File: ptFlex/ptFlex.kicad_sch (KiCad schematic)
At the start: 75 parts, among them J1 6 Pin Male Header, J2 8 Pin Male Header, J4 Qwiic, J5 3 Pin Male Header, J6 Barrel_Jack_Switch, Q1 BSS138, Q2 BSS138, Q3 MMBT3904, Q4 MMBT3904, Q5 DMP2004K-7, SW1 Reset Switch, U1 LP3985IM5-3.3/NOPB, U2 ATMega 328p-AU, U3 SA818S-V, U4 ATGM336H-5N31, U5 LM1086-5.0, U6 BME280, Y1 8MHz

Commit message: Schematic mostly revised for v2.0
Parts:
- removed ANT2a1, ANT2b1: VHF Test Point, Custom DS:Small Test Point Pin, symbol Connector_Generic:Conn_01x01
- removed J2: 8 Pin Male Header, Connector_PinHeader_2.54mm:PinHeader_2x04_P2.54mm_Vertical, symbol Connector_Generic:Conn_02x04_Odd_Even
- Y1: value 8MHz -> 16MHz
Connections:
- net +3.3V: no longer C12.1, R7.1, U2.18 (AVCC), U2.4 (VCC), U2.6 (VCC)
- net BATT-SENSE: no longer C2.1, R2.1, R3.2
- net GND: now also SW1.1 (A); no longer SW1.2 (B)
- net GPS-RX: no longer U4.2 (TXD)
- net GPS-TX: no longer U4.3 (RXD)
- net RESET: now also SW1.2 (B)
- net SCL: no longer R8.2
- net SDA: no longer R9.2
- net at C1.1, U5.3 (VI): now also D4.1 (K), R2.2; no longer J6.1
- net at Q2.2 (S), R12.1: now also U4.2 (TXD)
- net at C20.1, Q5.3 (D), U4.8 (VCC): now also C12.1
- net at Q1.2 (S), R10.1: now also U4.3 (RXD)
- net at J5.1 (Pin_1): now also U2.31 (PD1)
- net at J5.2 (Pin_2): now also U2.30 (PD0)
- net at J4.3 (Pin_3), U6.3 (SDI): now also R9.2
- net at J4.4 (Pin_4), U6.4 (SCK): now also R8.2
- net at D4.2 (A): now also J6.1
- net PIEZO: now reaches R1.2
- net +BATT renamed +5V
- net +5V: now also R7.1, U2.18 (AVCC), U2.4 (VCC), U2.6 (VCC); no longer D4.1 (K), R2.2
- new net: C2.1, R2.1, R3.2
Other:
- moved on the sheet: ANT1, ANT2, C1, C10, C11, C12, C13, C14, C15, C16, C17, C18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

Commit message: PCB nearing final
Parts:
- removed SW1: Reset Switch, Button_Switch_SMD:SW_SPST_PTS647_Sx38, symbol Switch:SW_SPST
- ANT2: value SMA Edge Mount (Optional) -> SMA Connector; footprint Connector_Coaxial:SMA_Samtec_SMA-J-P-H-ST-EM1_EdgeMount -> Connector_Coaxial:SMB_Jack_Vertical; Digikey CON-SMA-EDGE-S-ND -> (none)
- C21: value 2.2uF -> 47uF; Digikey 445-1420-1-ND -> (none); LCSC C107128 -> (none)
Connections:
- net BATT-SENSE: now also C2.1, R2.1, R3.2
- net DIG-PTT: no longer R20.2, R4.1, U2.32 (PD2)
- net GPS-RX: now also Q2.3 (D), R13.1
- net GPS-TX: now also Q1.3 (D), R11.1
- net PIEZO: now also U2.9 (PD5)
- net XMIT-POWERSAVE: now reaches R22.2, U2.2 (PD4), U3.6 (POWER_SAVE)
- net XMIT-TX-AUDIO: now reaches R16.1, U2.1 (PD3)
- net XMIT-TX: now reaches U2.13 (PB1), U3.16 (RX_DATA)
- net XMIT-RX: now reaches U2.14 (PB2), U3.17 (TX_DATA)
- new net XMIT-PTT: R20.2, R4.1, U2.32 (PD2)
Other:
- moved on the sheet: C2, C20, D4, J6, Q2, R12, R13, R2, R22, R3

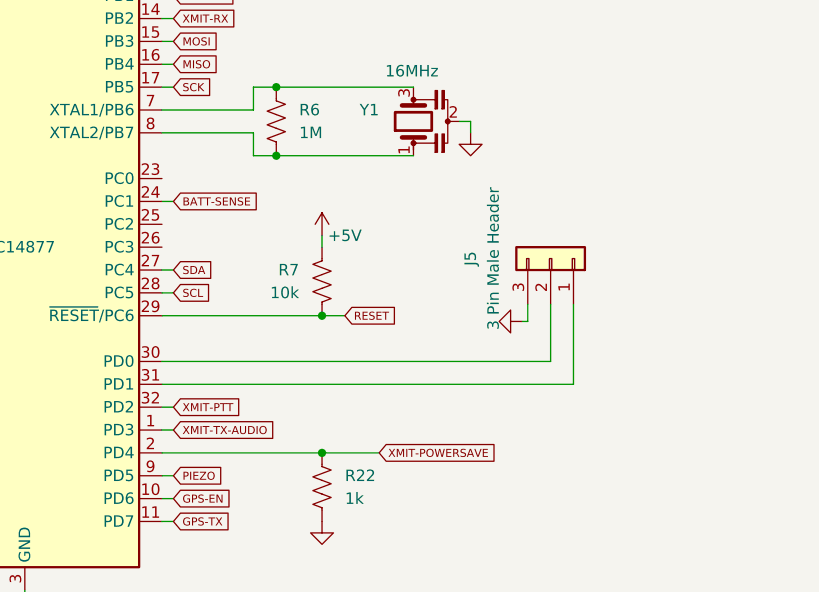
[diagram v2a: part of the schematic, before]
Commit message: Back filed old versions of PCB from the ptFlex-hardware project into this repo. Shrunk the PCB down by 5mm.
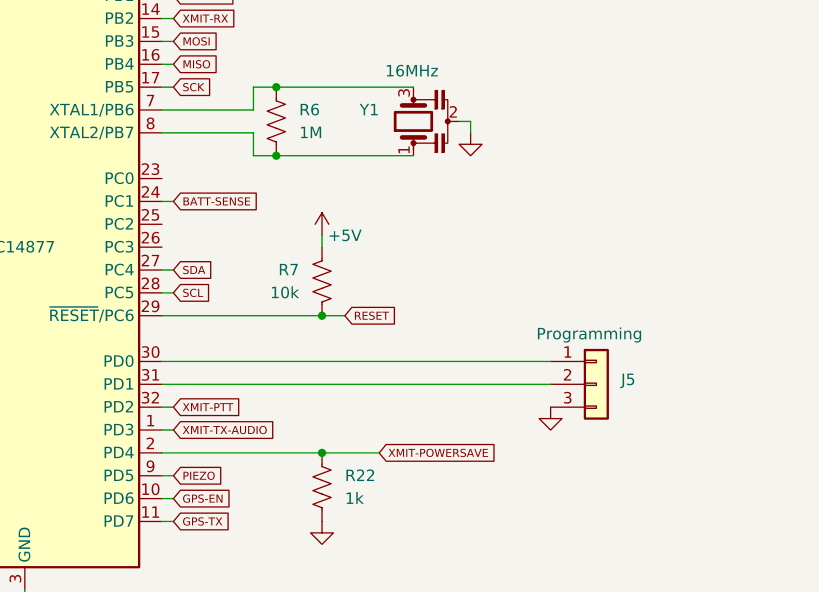
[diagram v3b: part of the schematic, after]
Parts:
- J5: value 3 Pin Male Header -> Programming
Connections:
- net at J5.1 (Pin_1): now also U2.30 (PD0); no longer U2.31 (PD1)
- net at J5.2 (Pin_2): now also U2.31 (PD1); no longer U2.30 (PD0)
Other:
- moved on the sheet: J5
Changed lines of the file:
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@@
 	(wire
 		(pts
-			(xy 163.83 67.31) (xy 163.83 69.215)
-		)
-		(stroke
-			(width 0)
-			(type default)
-		)
-	)
-	(wire
-		(pts
 			(xy 269.24 73.66) (xy 274.32 73.66)
 		)
@@
 	(wire
 		(pts
-			(xy 163.83 69.215) (xy 163.195 69.215)
-		)
-		(stroke
-			(width 0)
-			(type default)
-		)
-	)
-	(wire
-		(pts
 			(xy 36.83 48.26) (xy 36.83 52.07)
 		)
@@
 	(wire
 		(pts
-			(xy 166.37 67.31) (xy 166.37 73.66)
-		)
-		(stroke
-			(width 0)
-			(type default)
-		)
-	)
-	(wire
-		(pts
 			(xy 351.79 133.35) (xy 351.79 135.89)
 		)
@@
 	(wire
 		(pts
-			(xy 168.91 67.31) (xy 168.91 76.2)
-		)
-		(stroke
-			(width 0)
-			(type default)
-		)
-	)
-	(wire
-		(pts
-			(xy 123.19 76.2) (xy 168.91 76.2)
+			(xy 123.19 76.2) (xy 166.37 76.2)
 		)
 		(stroke
@@
 	(symbol
 		(lib_id "Connector_Generic:Conn_01x03")
-		(at 166.37 62.23 270)
-		(mirror x)
+		(at 171.45 76.2 0)
 		(unit 1)
 		(exclude_from_sim no)
@@
 		(dnp no)
 		(property "Reference" "J5"
-			(at 157.48 62.23 0)
+			(at 175.006 75.692 0)
 			(effects
 				(font
@@
 			)
 		)
-		(property "Value" "3 Pin Male Header"
-			(at 160.02 62.23 0)
+		(property "Value" "Programming"
+			(at 170.688 70.612 0)
 			(effects
 				(font
@@
 		)
 		(property "Footprint" "Connector_PinHeader_2.54mm:PinHeader_1x03_P2.54mm_Vertical"
-			(at 166.37 62.23 0)
+			(at 171.45 76.2 0)
 			(effects
 				(font
@@
 		)
 		(property "Datasheet" "~"
-			(at 166.37 62.23 0)
+			(at 171.45 76.2 0)
 			(effects
 				(font
@@
 		)
 		(property "Description" "Generic connector, single row, 01x03, script generated (kicad-library-utils/schlib/autogen/connector/)"
-			(at 166.37 62.23 0)
+			(at 171.45 76.2 0)
 			(effects
 				(font
@@
 		)
 		(property "Digikey" "732-5316-ND"
-			(at 166.37 62.23 0)
+			(at 171.45 76.2 0)
 			(effects
 				(font
@@
 		)
 		(property "LSCC" ""
-			(at 166.37 62.23 0)
+			(at 171.45 76.2 0)
 			(effects
 				(font
@@
 	)
 	(symbol
-		(lib_id "power:GND")
-		(at 163.195 69.215 270)
-		(unit 1)
-		(exclude_from_sim no)
-		(in_bom yes)
-		(on_board yes)
-		(dnp no)
-		(property "Reference" "#SUPPLY024"
-			(at 163.195 69.215 0)
-			(effects
-				(font
-					(size 1.27 1.27)
-				)
-				(hide yes)
-			)
-		)
-		(property "Value" "GND"
-			(at 161.163 70.739 0)
-			(effects
-				(font
-					(size 1.778 1.5113)
-				)
-				(justify left bottom)
-				(hide yes)
-			)
-		)
-		(property "Footprint" ""
-			(at 163.195 69.215 0)
-			(effects
-				(font
-					(size 1.27 1.27)
-				)
-				(hide yes)
-			)
-		)
-		(property "Datasheet" ""
-			(at 163.195 69.215 0)
-			(effects
-				(font
-					(size 1.27 1.27)
-				)
-				(hide yes)
-			)
-		)
-		(property "Description" "Power symbol creates a global label with name \"GND\" , ground"
-			(at 163.195 69.215 0)
-			(effects
-				(font
-					(size 1.27 1.27)
-				)
-				(hide yes)
-			)
-		)
-		(pin "1"
-		)
-		(instances
-			(project "ptFlex"
-				(path "/166d0a8f-2333-4a81-bfd6-a1b5ff84420a"
-					(reference "#SUPPLY024")
-					(unit 1)
-				)
-			)
-		)
-	)
-	(symbol
 		(lib_id "Device:R_US")
 		(at 177.8 200.66 180)
@@
 					(unit 1)
 				)
+			)
+		)
+	)
+	(symbol
+		(lib_id "power:GND")
+		(at 166.37 78.74 0)
+		(unit 1)
+		(exclude_from_sim no)
+		(in_bom yes)
+		(on_board yes)
+		(dnp no)
+		(property "Reference" "#SUPPLY024"
+			(at 166.37 78.74 0)
+			(effects
+				(font
+					(size 1.27 1.27)
+				)
+				(hide yes)
+			)
+		)
+		(property "Value" "GND"
+			(at 167.894 80.772 0)
+			(effects
+				(font
+					(size 1.778 1.5113)
+				)
+				(justify left bottom)
+				(hide yes)
+			)
+		)
+		(property "Footprint" ""
+			(at 166.37 78.74 0)
+			(effects
+				(font
+					(size 1.27 1.27)
+				)
+				(hide yes)
+			)
+		)
+		(property "Datasheet" ""
+			(at 166.37 78.74 0)
+			(effects
+				(font
+					(size 1.27 1.27)
+				)
+				(hide yes)
+			)
+		)
+		(property "Description" "Power symbol creates a global label with name \"GND\" , ground"
+			(at 166.37 78.74 0)
+			(effects
+				(font
+					(size 1.27 1.27)
+				)
+				(hide yes)
+			)
+		)
+		(pin "1"
+		)
+		(instances
+			(project "ptFlex"
+				(path "/166d0a8f-2333-4a81-bfd6-a1b5ff84420a"
+					(reference "#SUPPLY024")
+					(unit 1)
+				)

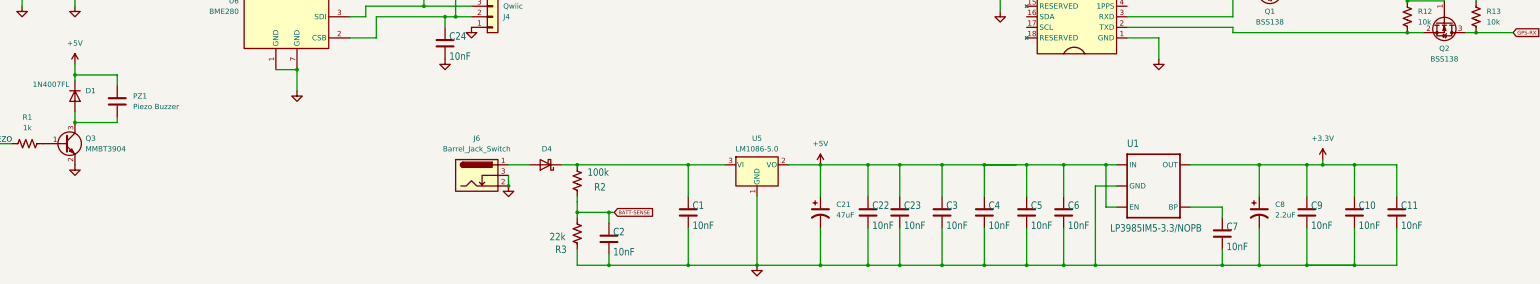
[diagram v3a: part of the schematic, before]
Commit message: Swapped out Piezo symbol. Minor tweaks
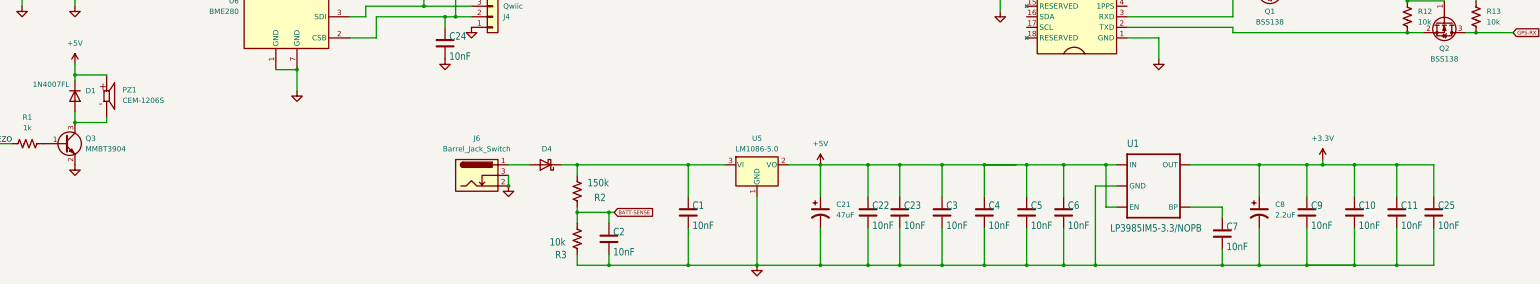
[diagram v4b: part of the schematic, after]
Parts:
- removed PZ1: Piezo Buzzer, Buzzer_Beeper:Buzzer_TDK_PS1240P02BT_D12.2mm_H6.5mm, symbol Device:C
- added C25: 10nF, Capacitor_SMD:C_0805_2012Metric, symbol Device:C
- added PZ1: CEM-1206S, CUI_CEM-1206S, symbol CEM-1206S:CEM-1206S
- R2: value 100k -> 150k; Digikey 311-100KCRCT-ND -> 311-150KARCT-ND; LCSC C96346 -> 17470
- R3: value 22k -> 10k; Digikey 311-22KARTR-ND -> 311-10KARCT-ND; LCSC C104107 -> C110775
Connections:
- net +3.3V: now also C25.1
- net +5V: now also PZ1.P
- net GND: now also C25.2
- net at D1.2 (A), Q3.3 (C): now also PZ1.N
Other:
- moved on the sheet: R2, R3

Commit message: Renumbered all parts.
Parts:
- C3: renamed from C21; Digikey (none) -> 399-C0805C476M9PACTUCT-ND; LCSC (none) -> C16780
- renumbered C7 to C10, C8 to C11, C9 to C12, C10 to C13, C11 to C14, C25 to C15, C24 to C16, C15 to C17, C14 to C18, C12 to C19, C16 to C21, C17 to C22, C18 to C23, C19 to C24, C13 to C25, C22 to C4, C23 to C5, C3 to C6, C4 to C7, C5 to C8, C6 to C9, D4 to D1, D5 to D2, D6 to D3, D1 to D4, J6 to J1, J5 to J2, J4 to J3, J1 to J4, Q3 to Q1, Q4 to Q2, Q5 to Q3, Q1 to Q4, Q2 to Q5, R2 to R1, R22 to R10, R20 to R11, R21 to R12, R16 to R13, R17 to R14, R18 to R15, R19 to R16, R23 to R17, R10 to R18, R11 to R19, R3 to R2, R12 to R20, R13 to R21, R4 to R3, R5 to R4, R1 to R5, R8 to R6, R9 to R7, R6 to R8, R7 to R9, U5 to U1, U1 to U2, U2 to U3, U3 to U5

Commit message: Finalized version 2.0.0 of the PCB to bring it in sync with the ptSolar design.
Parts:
- PZ1: MP CEM-1206S -> (none)
- R1: LCSC 17470 -> C17470
- Y1: Digikey 490-CSTNE8M00G520000R0CT-ND -> 490-17948-2-ND; LCSC C907975 -> C341521
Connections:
- net DIG-PTT is gone; now on net XMIT-PTT: R14.1
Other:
- moved on the sheet: ANT1, ANT2, C16, C17, C18, C19, C20, C21, C22, C23, C24, C25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

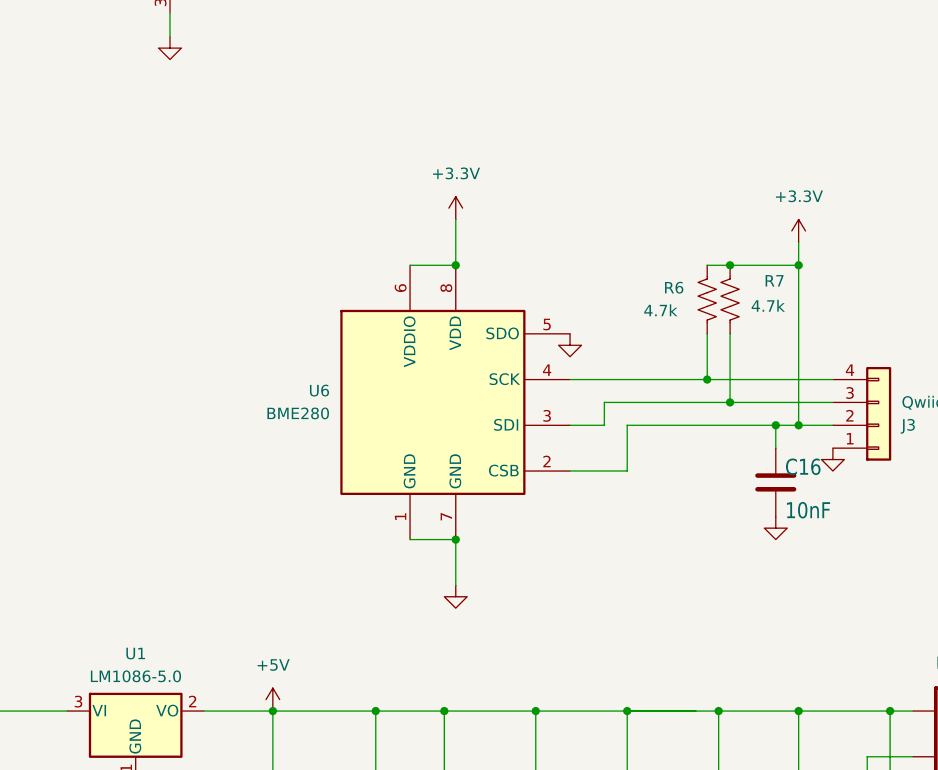
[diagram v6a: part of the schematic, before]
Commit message: Board redesigned to 2.0.1 to fix missing SDA/SCL pins to uC. Shrunk board slightly. Fixed SMA center hole being too small.
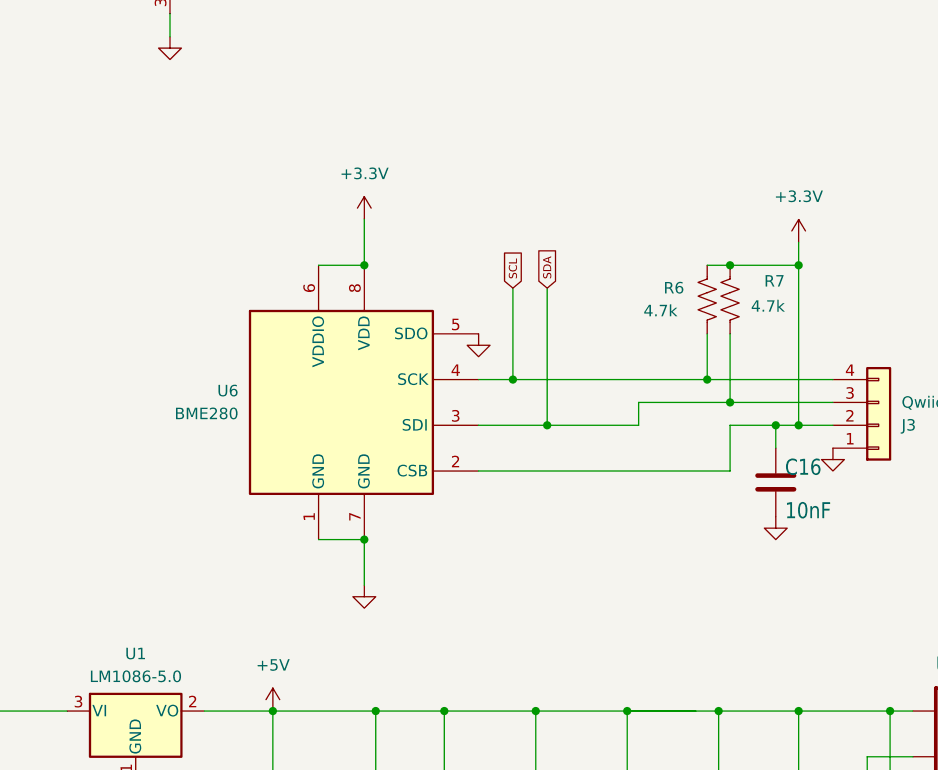
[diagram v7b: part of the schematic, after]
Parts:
- removed PZ1: CEM-1206S, CUI_CEM-1206S, symbol CEM-1206S:CEM-1206S
- added PZ1: CEM-1206S, Custom DS:CUI_CEM-1206S, symbol Custom DS:PIezo CEM-1206S
- ANT2: footprint Connector_Coaxial:SMB_Jack_Vertical -> Custom DS:SMA_Thru_Hole
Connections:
- net +5V: now also PZ1.P
- net SCL: now also J3.4 (Pin_4), R6.2, U6.4 (SCK)
- net SDA: now also J3.3 (Pin_3), R7.2, U6.3 (SDI)
- net at D4.2 (A), Q1.3 (C): now also PZ1.N
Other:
- moved on the sheet: U6

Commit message: Adjusting voltage divider resistor precision.
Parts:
- R1: Digikey 311-150KARCT-ND -> 311-150KCRCT-ND; LCSC C17470 -> C114558
- R11, R12, R15, R16, R17, R18, R19, R2, R20, R21, R9: Digikey 311-10KARCT-ND -> 13-RT0805FRD0710KLCT-ND; LCSC C110775 -> C100047
